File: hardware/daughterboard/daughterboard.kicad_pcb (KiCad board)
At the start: 2 copper layers, 101.8 x 103.5 mm, 8 parts, among them J1 Conn_01x08, J2 Conn_01x02, J3 Conn_01x04, J4 Conn_01x08

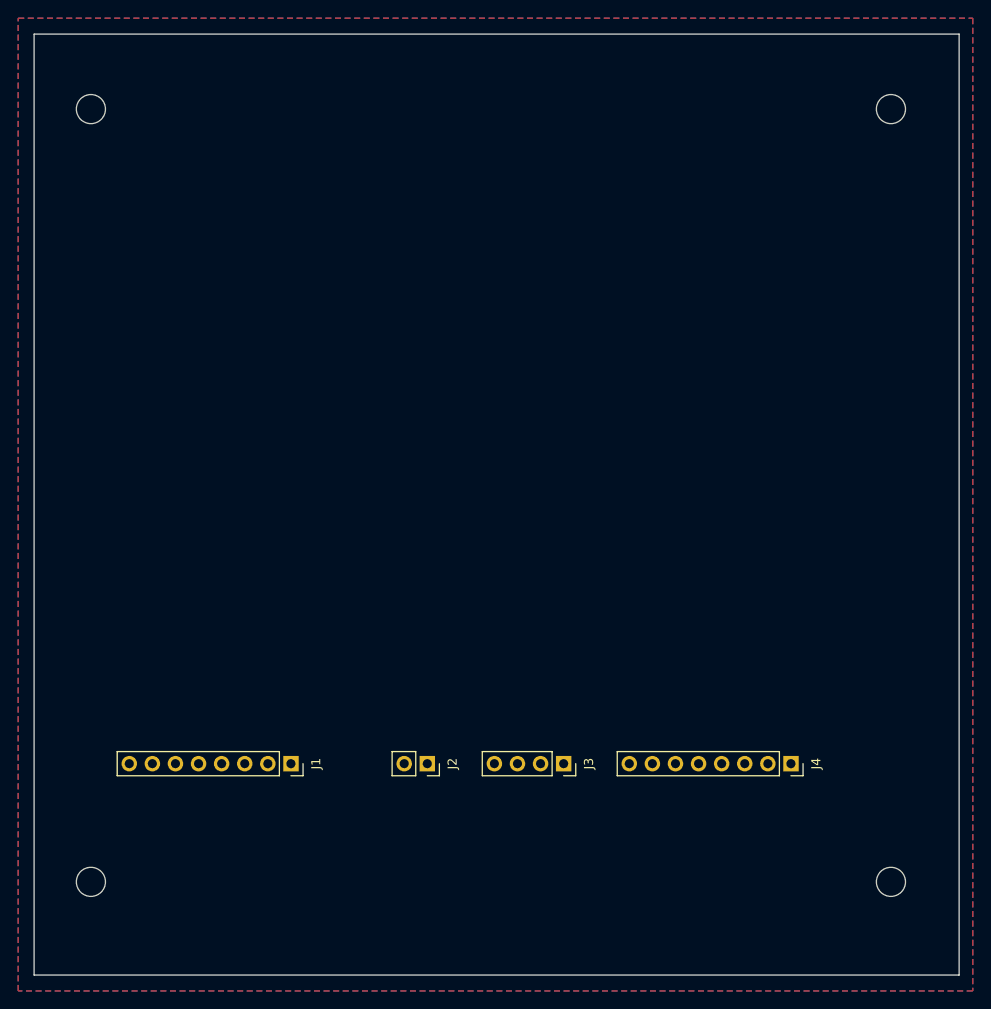
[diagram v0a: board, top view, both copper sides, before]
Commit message: Daughterboard edge adjustments, pdf and png
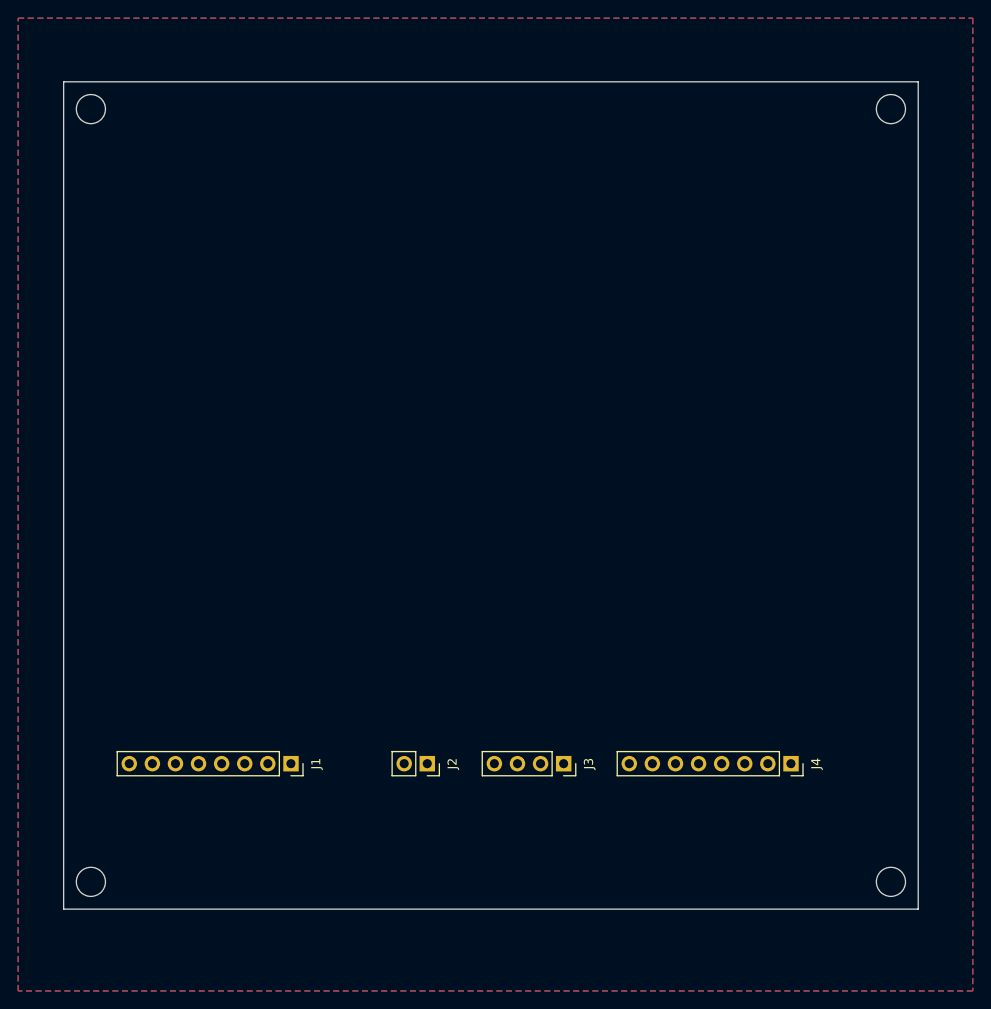
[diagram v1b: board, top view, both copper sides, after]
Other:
- board size 101.8 x 103.5 mm -> 94 x 91 mm
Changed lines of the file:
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@@
   (general
     (thickness 1.6)
-    (drawings 4)
+    (drawings 6)
     (tracks 0)
     (zones 0)
@@
     (pad 1 np_thru_hole circle (at 0 0) (size 3.2 3.2) (drill 3.2) (layers *.Cu *.Mask))
   )
-  (gr_line (start 136.75 148.25) (end 136.75 44.75) (layer Edge.Cuts) (width 0.05))
-  (gr_line (start 238.5 148.25) (end 136.75 148.25) (layer Edge.Cuts) (width 0.05))
-  (gr_line (start 238.5 44.75) (end 238.5 148.25) (layer Edge.Cuts) (width 0.05))
-  (gr_line (start 136.75 44.75) (end 238.5 44.75) (layer Edge.Cuts) (width 0.05))
+  (dimension 94 (width 0.15) (layer Dwgs.User)
+    (gr_text "94.000 mm" (at 187 61.3) (layer Dwgs.User)
+      (effects (font (size 1 1) (thickness 0.15)))
+    )
+    (feature1 (pts (xy 234 50) (xy 234 60.586421)))
+    (feature2 (pts (xy 140 50) (xy 140 60.586421)))
+    (crossbar (pts (xy 140 60) (xy 234 60)))
+    (arrow1a (pts (xy 234 60) (xy 232.873496 60.586421)))
+    (arrow1b (pts (xy 234 60) (xy 232.873496 59.413579)))
+    (arrow2a (pts (xy 140 60) (xy 141.126504 60.586421)))
+    (arrow2b (pts (xy 140 60) (xy 141.126504 59.413579)))
+  )
+  (dimension 91 (width 0.15) (layer Dwgs.User)
+    (gr_text "91.000 mm" (at 223.7 95.5 270) (layer Dwgs.User)
+      (effects (font (size 1 1) (thickness 0.15)))
+    )
+    (feature1 (pts (xy 234 141) (xy 224.413579 141)))
+    (feature2 (pts (xy 234 50) (xy 224.413579 50)))
+    (crossbar (pts (xy 225 50) (xy 225 141)))
+    (arrow1a (pts (xy 225 141) (xy 224.413579 139.873496)))
+    (arrow1b (pts (xy 225 141) (xy 225.586421 139.873496)))
+    (arrow2a (pts (xy 225 50) (xy 224.413579 51.126504)))
+    (arrow2b (pts (xy 225 50) (xy 225.586421 51.126504)))
+  )
+  (gr_line (start 140 141) (end 140 50) (layer Edge.Cuts) (width 0.05))
+  (gr_line (start 234 141) (end 140 141) (layer Edge.Cuts) (width 0.05))
+  (gr_line (start 234 50) (end 234 141) (layer Edge.Cuts) (width 0.05))
+  (gr_line (start 140 50) (end 234 50) (layer Edge.Cuts) (width 0.05))
   (zone (net 21) (net_name GND) (layer F.Cu) (hatch edge 0.508)
     (connect_pads (clearance 0.508))

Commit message: Pin labels
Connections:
- net Net-(J1-Pad3) renamed /GATE_OUT_B
- net Net-(J1-Pad4) renamed /GATE_OUT_A
- net Net-(J1-Pad5) renamed /GATE_IN_D
- net Net-(J1-Pad6) renamed /GATE_IN_C
- net Net-(J1-Pad7) renamed /GATE_IN_B
- net Net-(J1-Pad8) renamed /GATE_IN_A
- net Net-(J2-Pad1) renamed /D8
- net Net-(J2-Pad2) renamed /D9
- net Net-(J3-Pad1) renamed /A7
- net Net-(J3-Pad2) renamed /A6
- net Net-(J3-Pad3) renamed /A5
- net Net-(J3-Pad4) renamed /A4
- net Net-(J4-Pad1) renamed /CV_IN_A
- net Net-(J4-Pad2) renamed /CV_IN_B
- net Net-(J4-Pad3) renamed /CV_IN_C
- net Net-(J4-Pad4) renamed /CV_IN_D
- net Net-(J4-Pad5) renamed /CV_OUT_A
- net Net-(J4-Pad6) renamed /CV_OUT_B
- J1 pad 2: Net-(J1-Pad2) -> VCC
- J4 pad 7: Net-(J4-Pad7) -> VCC
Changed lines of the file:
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@@
     (zones 0)
     (modules 8)
-    (nets 22)
+    (nets 21)
   )
   (page A4)
@@
   )
   (net 0 "")
-  (net 1 "Net-(J1-Pad8)")
-  (net 2 "Net-(J1-Pad7)")
-  (net 3 "Net-(J1-Pad6)")
-  (net 4 "Net-(J1-Pad5)")
-  (net 5 "Net-(J1-Pad4)")
-  (net 6 "Net-(J1-Pad3)")
-  (net 7 "Net-(J1-Pad2)")
-  (net 8 "Net-(J2-Pad2)")
-  (net 9 "Net-(J2-Pad1)")
-  (net 10 "Net-(J3-Pad4)")
-  (net 11 "Net-(J3-Pad3)")
-  (net 12 "Net-(J3-Pad2)")
-  (net 13 "Net-(J3-Pad1)")
-  (net 14 "Net-(J4-Pad7)")
-  (net 15 "Net-(J4-Pad6)")
-  (net 16 "Net-(J4-Pad5)")
-  (net 17 "Net-(J4-Pad4)")
-  (net 18 "Net-(J4-Pad3)")
-  (net 19 "Net-(J4-Pad2)")
-  (net 20 "Net-(J4-Pad1)")
-  (net 21 GND)
+  (net 1 GND)
+  (net 2 /GATE_IN_A)
+  (net 3 /GATE_IN_B)
+  (net 4 /GATE_IN_C)
+  (net 5 /GATE_IN_D)
+  (net 6 /GATE_OUT_A)
+  (net 7 /GATE_OUT_B)
+  (net 8 VCC)
+  (net 9 /D9)
+  (net 10 /D8)
+  (net 11 /A4)
+  (net 12 /A5)
+  (net 13 /A6)
+  (net 14 /A7)
+  (net 15 /CV_OUT_B)
+  (net 16 /CV_OUT_A)
+  (net 17 /CV_IN_D)
+  (net 18 /CV_IN_C)
+  (net 19 /CV_IN_B)
+  (net 20 /CV_IN_A)
   (net_class Default "This is the default net class."
     (clearance 0.2)
@@
     (uvia_dia 0.3)
     (uvia_drill 0.1)
+    (add_net /A4)
+    (add_net /A5)
+    (add_net /A6)
+    (add_net /A7)
+    (add_net /CV_IN_A)
+    (add_net /CV_IN_B)
+    (add_net /CV_IN_C)
+    (add_net /CV_IN_D)
+    (add_net /CV_OUT_A)
+    (add_net /CV_OUT_B)
+    (add_net /D8)
+    (add_net /D9)
+    (add_net /GATE_IN_A)
+    (add_net /GATE_IN_B)
+    (add_net /GATE_IN_C)
+    (add_net /GATE_IN_D)
+    (add_net /GATE_OUT_A)
+    (add_net /GATE_OUT_B)
     (add_net GND)
-    (add_net "Net-(J1-Pad2)")
-    (add_net "Net-(J1-Pad3)")
-    (add_net "Net-(J1-Pad4)")
-    (add_net "Net-(J1-Pad5)")
-    (add_net "Net-(J1-Pad6)")
-    (add_net "Net-(J1-Pad7)")
-    (add_net "Net-(J1-Pad8)")
-    (add_net "Net-(J2-Pad1)")
-    (add_net "Net-(J2-Pad2)")
-    (add_net "Net-(J3-Pad1)")
-    (add_net "Net-(J3-Pad2)")
-    (add_net "Net-(J3-Pad3)")
-    (add_net "Net-(J3-Pad4)")
-    (add_net "Net-(J4-Pad1)")
-    (add_net "Net-(J4-Pad2)")
-    (add_net "Net-(J4-Pad3)")
-    (add_net "Net-(J4-Pad4)")
-    (add_net "Net-(J4-Pad5)")
-    (add_net "Net-(J4-Pad6)")
-    (add_net "Net-(J4-Pad7)")
+    (add_net VCC)
   )
   (module Connector_PinSocket_2.54mm:PinSocket_1x08_P2.54mm_Vertical locked (layer F.Cu)
@@
     (fp_line (start -1.27 -1.27) (end 0.635 -1.27) (layer F.Fab) (width 0.1))
     (pad 8 thru_hole oval (at 0 17.78 270) (size 1.7 1.7) (drill 1) (layers *.Cu *.Mask)
-      (net 21 GND))
+      (net 1 GND))
     (pad 7 thru_hole oval (at 0 15.24 270) (size 1.7 1.7) (drill 1) (layers *.Cu *.Mask)
-      (net 14 "Net-(J4-Pad7)"))
+      (net 8 VCC))
     (pad 6 thru_hole oval (at 0 12.7 270) (size 1.7 1.7) (drill 1) (layers *.Cu *.Mask)
-      (net 15 "Net-(J4-Pad6)"))
+      (net 15 /CV_OUT_B))
     (pad 5 thru_hole oval (at 0 10.16 270) (size 1.7 1.7) (drill 1) (layers *.Cu *.Mask)
-      (net 16 "Net-(J4-Pad5)"))
+      (net 16 /CV_OUT_A))
     (pad 4 thru_hole oval (at 0 7.62 270) (size 1.7 1.7) (drill 1) (layers *.Cu *.Mask)
-      (net 17 "Net-(J4-Pad4)"))
+      (net 17 /CV_IN_D))
     (pad 3 thru_hole oval (at 0 5.08 270) (size 1.7 1.7) (drill 1) (layers *.Cu *.Mask)
-      (net 18 "Net-(J4-Pad3)"))
+      (net 18 /CV_IN_C))
     (pad 2 thru_hole oval (at 0 2.54 270) (size 1.7 1.7) (drill 1) (layers *.Cu *.Mask)
-      (net 19 "Net-(J4-Pad2)"))
+      (net 19 /CV_IN_B))
     (pad 1 thru_hole rect (at 0 0 270) (size 1.7 1.7) (drill 1) (layers *.Cu *.Mask)
-      (net 20 "Net-(J4-Pad1)"))
+      (net 20 /CV_IN_A))
     (model ${KISYS3DMOD}/Connector_PinSocket_2.54mm.3dshapes/PinSocket_1x08_P2.54mm_Vertical.wrl
       (at (xyz 0 0 0))
@@
     (fp_line (start -1.27 -1.27) (end 0.635 -1.27) (layer F.Fab) (width 0.1))
     (pad 4 thru_hole oval (at 0 7.62 270) (size 1.7 1.7) (drill 1) (layers *.Cu *.Mask)
-      (net 10 "Net-(J3-Pad4)"))
+      (net 11 /A4))
     (pad 3 thru_hole oval (at 0 5.08 270) (size 1.7 1.7) (drill 1) (layers *.Cu *.Mask)
-      (net 11 "Net-(J3-Pad3)"))
+      (net 12 /A5))
     (pad 2 thru_hole oval (at 0 2.54 270) (size 1.7 1.7) (drill 1) (layers *.Cu *.Mask)
-      (net 12 "Net-(J3-Pad2)"))
+      (net 13 /A6))
     (pad 1 thru_hole rect (at 0 0 270) (size 1.7 1.7) (drill 1) (layers *.Cu *.Mask)
-      (net 13 "Net-(J3-Pad1)"))
+      (net 14 /A7))
     (model ${KISYS3DMOD}/Connector_PinSocket_2.54mm.3dshapes/PinSocket_1x04_P2.54mm_Vertical.wrl
       (at (xyz 0 0 0))
@@
     (fp_line (start -1.27 -1.27) (end 0.635 -1.27) (layer F.Fab) (width 0.1))
     (pad 2 thru_hole oval (at 0 2.54 270) (size 1.7 1.7) (drill 1) (layers *.Cu *.Mask)
-      (net 8 "Net-(J2-Pad2)"))
+      (net 9 /D9))
     (pad 1 thru_hole rect (at 0 0 270) (size 1.7 1.7) (drill 1) (layers *.Cu *.Mask)
-      (net 9 "Net-(J2-Pad1)"))
+      (net 10 /D8))
     (model ${KISYS3DMOD}/Connector_PinSocket_2.54mm.3dshapes/PinSocket_1x02_P2.54mm_Vertical.wrl
       (at (xyz 0 0 0))
@@
     (fp_line (start -1.27 -1.27) (end 0.635 -1.27) (layer F.Fab) (width 0.1))
     (pad 8 thru_hole oval (at 0 17.78 270) (size 1.7 1.7) (drill 1) (layers *.Cu *.Mask)
-      (net 1 "Net-(J1-Pad8)"))
+      (net 2 /GATE_IN_A))
     (pad 7 thru_hole oval (at 0 15.24 270) (size 1.7 1.7) (drill 1) (layers *.Cu *.Mask)
-      (net 2 "Net-(J1-Pad7)"))
+      (net 3 /GATE_IN_B))
     (pad 6 thru_hole oval (at 0 12.7 270) (size 1.7 1.7) (drill 1) (layers *.Cu *.Mask)
-      (net 3 "Net-(J1-Pad6)"))
+      (net 4 /GATE_IN_C))
     (pad 5 thru_hole oval (at 0 10.16 270) (size 1.7 1.7) (drill 1) (layers *.Cu *.Mask)
-      (net 4 "Net-(J1-Pad5)"))
+      (net 5 /GATE_IN_D))
     (pad 4 thru_hole oval (at 0 7.62 270) (size 1.7 1.7) (drill 1) (layers *.Cu *.Mask)
-      (net 5 "Net-(J1-Pad4)"))
+      (net 6 /GATE_OUT_A))
     (pad 3 thru_hole oval (at 0 5.08 270) (size 1.7 1.7) (drill 1) (layers *.Cu *.Mask)
-      (net 6 "Net-(J1-Pad3)"))
+      (net 7 /GATE_OUT_B))
     (pad 2 thru_hole oval (at 0 2.54 270) (size 1.7 1.7) (drill 1) (layers *.Cu *.Mask)
-      (net 7 "Net-(J1-Pad2)"))
+      (net 8 VCC))
     (pad 1 thru_hole rect (at 0 0 270) (size 1.7 1.7) (drill 1) (layers *.Cu *.Mask)
-      (net 21 GND))
+      (net 1 GND))
     (model ${KISYS3DMOD}/Connector_PinSocket_2.54mm.3dshapes/PinSocket_1x08_P2.54mm_Vertical.wrl
       (at (xyz 0 0 0))
@@
   (gr_line (start 234 50) (end 234 141) (layer Edge.Cuts) (width 0.05))
   (gr_line (start 140 50) (end 234 50) (layer Edge.Cuts) (width 0.05))
-  (zone (net 21) (net_name GND) (layer F.Cu) (hatch edge 0.508)
+  (zone (net 1) (net_name GND) (layer F.Cu) (hatch edge 0.508)
     (connect_pads (clearance 0.508))
     (min_thickness 0.254)
@@
     )
   )
-  (zone (net 21) (net_name GND) (layer B.Cu) (hatch edge 0.508)
+  (zone (net 1) (net_name GND) (layer B.Cu) (hatch edge 0.508)
     (connect_pads (clearance 0.508))
     (min_thickness 0.254)
